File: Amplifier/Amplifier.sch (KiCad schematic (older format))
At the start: 12 parts

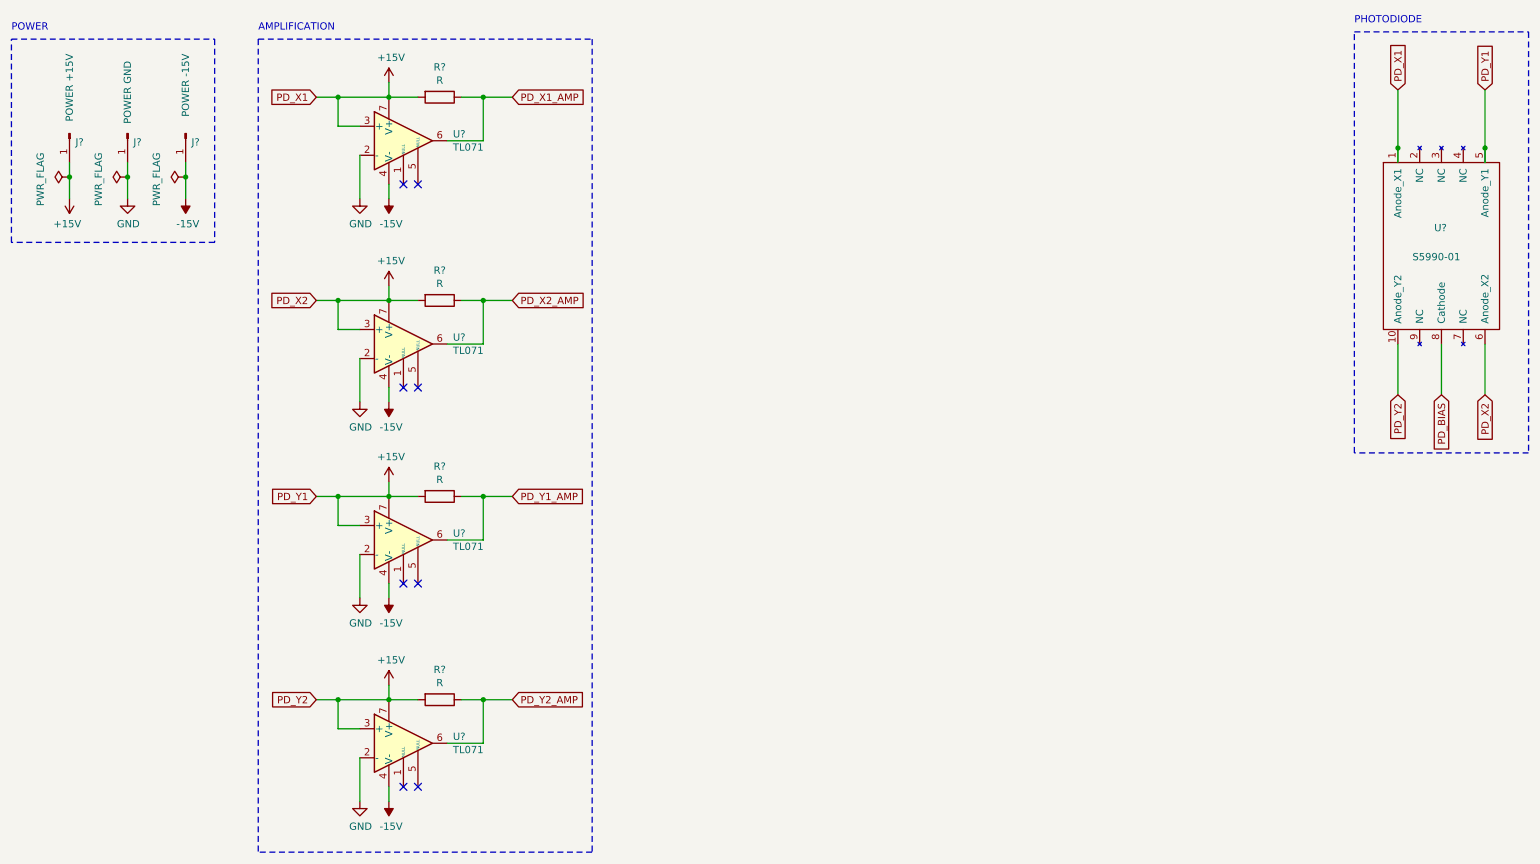
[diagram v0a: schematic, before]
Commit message: completed difference and summation stages
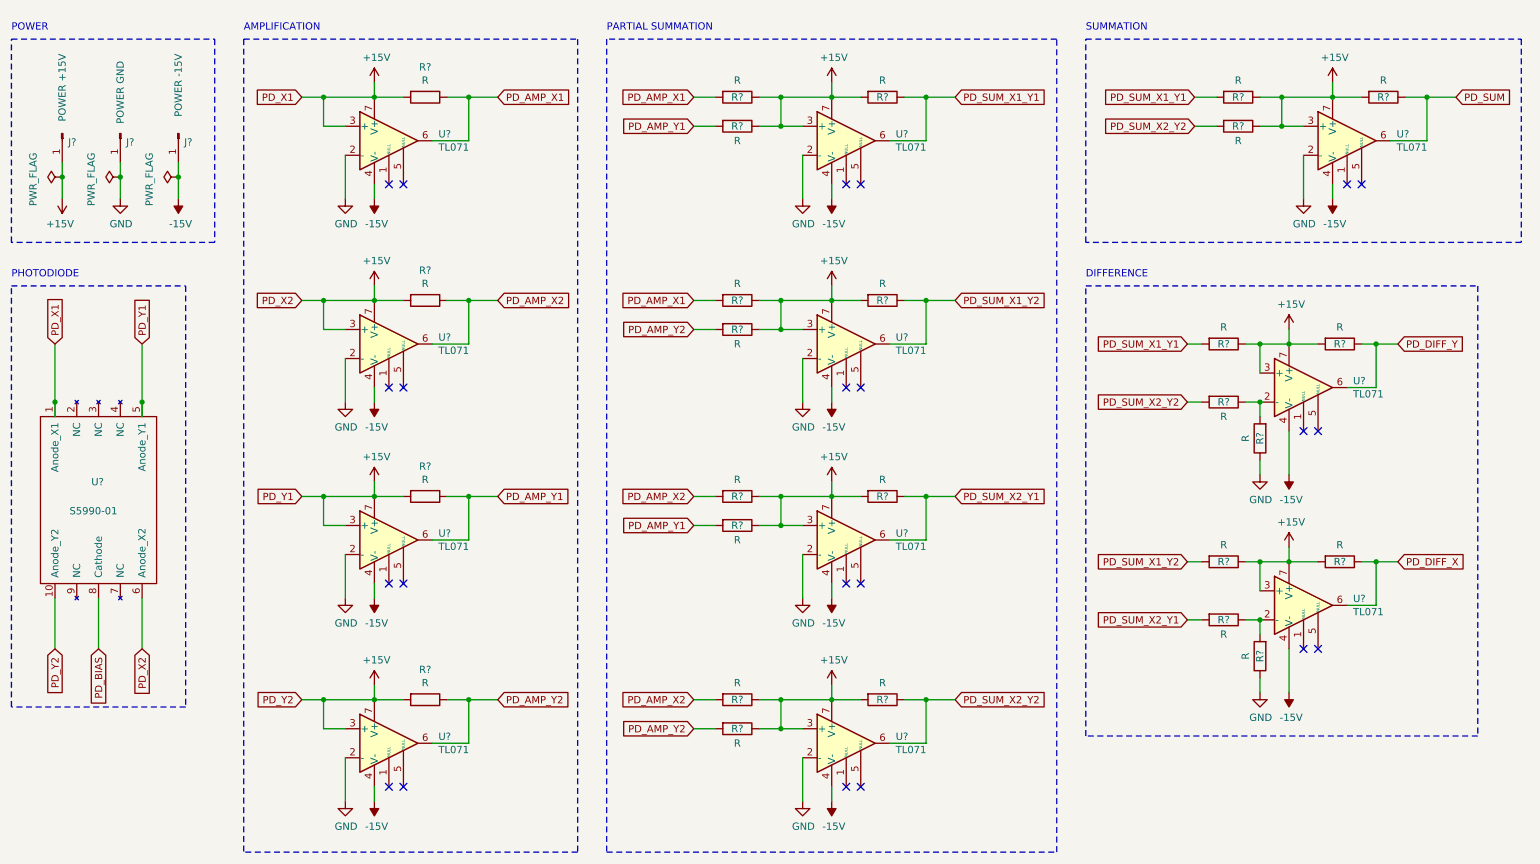
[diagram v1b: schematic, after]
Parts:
- added R? (x23): R, symbol Device:R
- added U? (x7): TL071, symbol Amplifier_Operational:TL071
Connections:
- net labels added: PD_AMP_X1, PD_AMP_X2, PD_AMP_Y1, PD_AMP_Y2, PD_DIFF_X, PD_DIFF_Y, PD_SUM, PD_SUM_X1_Y1, PD_SUM_X1_Y2, PD_SUM_X2_Y1, PD_SUM_X2_Y2
- net labels removed: PD_X1_AMP, PD_X2_AMP, PD_Y1_AMP, PD_Y2_AMP
- wire segments 61 -> 166
- no-connect marks 8 -> 22
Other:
- note added: "DIFFERENCE"
- note added: "PARTIAL SUMMATION"
- note added: "SUMMATION"
- moved on the sheet: J?, R?, U?

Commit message: redesigned blocks for space efficiency
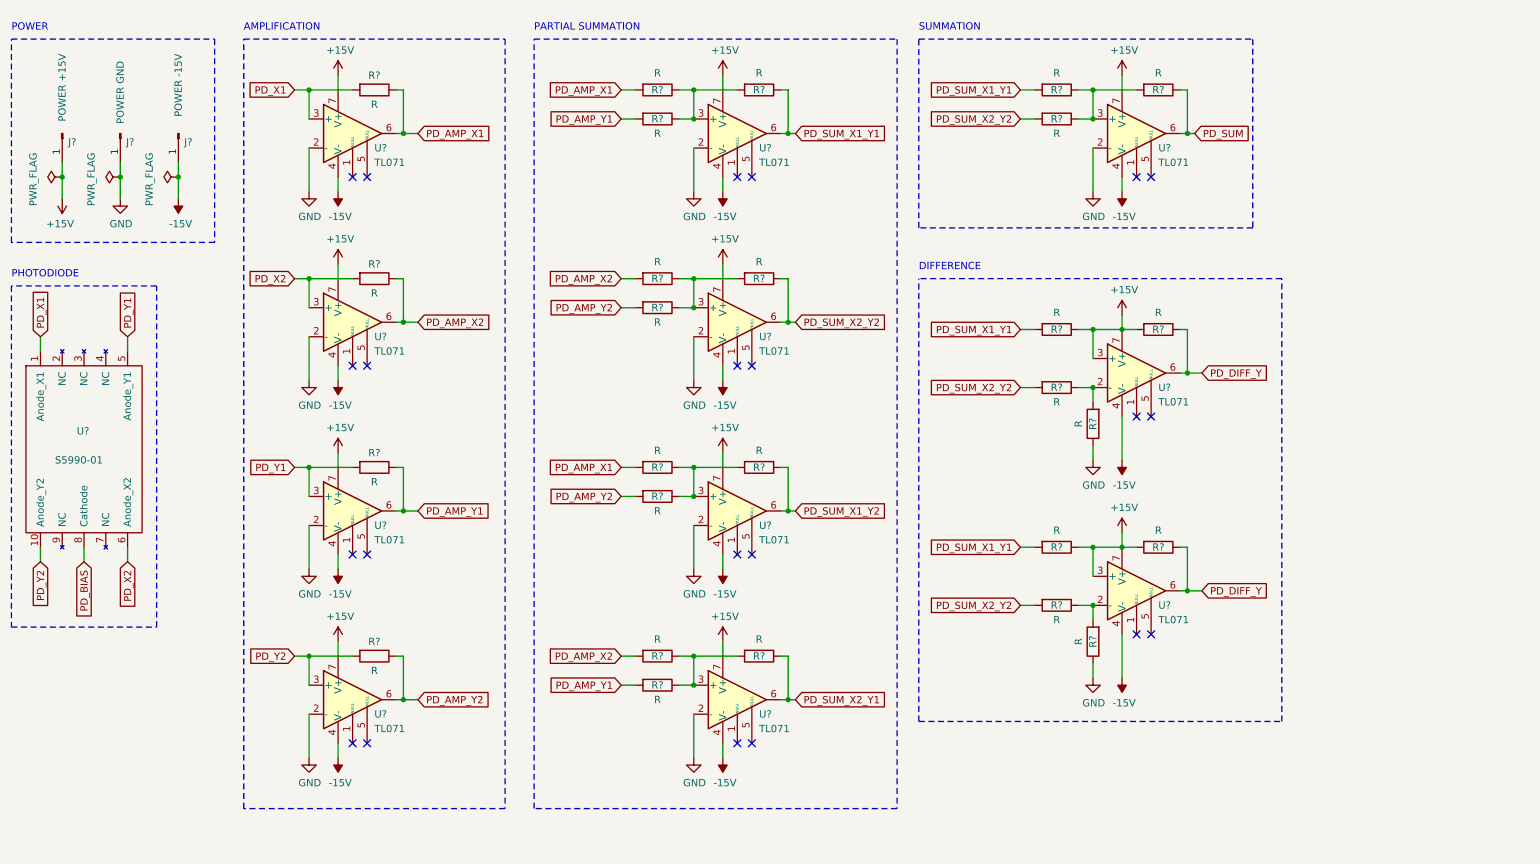
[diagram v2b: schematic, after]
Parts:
- removed R? (x19): R, symbol Device:R
- removed U? (x8): TL071, symbol Amplifier_Operational:TL071
- added R? (x19): R, symbol Device:R
- added U? (x8): TL071, symbol Amplifier_Operational:TL071
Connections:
- net +15V: now also R?.1, R?.2, U?.3 (+), U?.7 (V+), U?.7 (V+), U?.7 (V+), U?.7 (V+), U?.7 (V+), U?.7 (V+), U?.7 (V+), U?.7 (V+); no longer R?.1, R?.1, R?.2, R?.2, U?.1 (Anode_X1), U?.10 (Anode_Y2), U?.3 (+), U?.3 (+), U?.5 (Anode_Y1), U?.6 (Anode_X2)
- net -15V: now also U?.4 (V-), U?.4 (V-), U?.4 (V-), U?.4 (V-), U?.4 (V-), U?.4 (V-), U?.4 (V-), U?.4 (V-)
- net GND: now also R?.1, U?.2 (-), U?.2 (-), U?.2 (-), U?.2 (-), U?.2 (-), U?.2 (-), U?.2 (-)
- net PD_AMP_X1: now also R?.2
- net PD_AMP_X2: now also R?.1, R?.2, R?.2, U?.6
- net PD_AMP_Y1: now also R?.1, R?.2, U?.6
- net PD_AMP_Y2: now also R?.1, R?.2, R?.2, U?.6
- net PD_DIFF_Y: now also R?.1, U?.6
- net PD_SUM: now also R?.1, U?.6
- net PD_SUM_X1_Y1: now also R?.2, R?.2
- net PD_SUM_X1_Y2: now also R?.1, U?.6
- net PD_SUM_X2_Y1: now also R?.1, U?.6
- net PD_SUM_X2_Y2: now also R?.1, R?.2, R?.2, U?.6
- new net: R?.1, R?.1, R?.2, U?.3 (+) (x5)
- new net: R?.1, R?.2, U?.2 (-)
- new net PD_X1: R?.2, U?.1 (Anode_X1), U?.3 (+)
- new net PD_X2: R?.2, U?.3 (+), U?.6 (Anode_X2)
- new net PD_Y1: R?.2, U?.3 (+), U?.5 (Anode_Y1)
- new net PD_Y2: R?.2, U?.10 (Anode_Y2), U?.3 (+)
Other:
- moved on the sheet: R?, U?
